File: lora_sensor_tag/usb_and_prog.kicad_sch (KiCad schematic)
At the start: 0 parts

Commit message: lora_sensor_tag: Update shematic
Update schematic with the following changes:
 - Add SX1276 LoRa modem schematic;
 - Add antenna matching network for SX1276 LoRa modem;
 - Add PE4259 RF switch for SX1276 LoRa modem;
 - Add USB-C connector;
 - Add CP2102 USB-to-UART bridge and programming interface;

Signed-off-by: Volodymyr <volodymyrnoha99@gmail.com>
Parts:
- added C39: C, symbol Device:C
- added D1, D2, D3: 1N630xCA, Diode_THT:D_DO-201AE_P15.24mm_Horizontal, symbol Diode:1N630xCA
- added J3: USB_C_Receptacle_USB2.0_14P, Package_DFN_QFN:Texas_RNQ0040A_WQFN-40-1EP_6x4mm_P0.4mm_EP4.7x2.7mm, symbol Connector:USB_C_Receptacle_USB2.0_14P
- added Q1: NPN, Package_DFN_QFN:Nordic_AQFN-94-1EP_7x7mm_P0.4mm, symbol Simulation_SPICE:NPN
- added Q2: NPN, symbol Simulation_SPICE:NPN
- added R18, R19, R20, R21, R22, R23: R, Package_DFN_QFN:QFN-24-1EP_4x4mm_P0.5mm_EP2.6x2.6mm, symbol Device:R
- added U10: CP2102N-Axx-xQFN28, Package_DFN_QFN:QFN-28-1EP_5x5mm_P0.5mm_EP3.35x3.35mm, symbol Interface_USB:CP2102N-Axx-xQFN28
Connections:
- new net: Q1.2 (B), R22.2
- new net: R20.1, R21.2, U10.8 (VBUS)
- new net: Q2.2 (B), R23.2
- new net: R18.2, U10.9 (~{RST})
- new net: R19.1, U10.11 (~{SUSPEND})
- new net 3V3: C39.1, R18.1, U10.6 (VDD), U10.7 (VREGIN)
- new net DTR: Q2.3 (E), R22.1, U10.28 (~{DTR})
- new net GND: C39.2, D1.1 (A1), D2.1 (A1), D3.1 (A1), J3.A1 (GND), J3.A12 (GND), J3.B1 (GND), J3.B12 (GND), J3.SH (SHIELD), R19.2, R21.1, U10.29 (GND), U10.3 (GND)
- new net MCU_EN: Q1.1 (C)
- new net MCU_IO0: Q2.1 (C)
- new net MCU_RX: U10.25 (RXD)
- new net MCU_TX: U10.26 (TXD)
- new net RTS: Q1.3 (E), R23.1, U10.24 (~{RTS})
- new net USB_D_M: D2.2 (A2), J3.A7 (D-), J3.B7 (D-), U10.5 (D-)
- new net USB_D_P: D1.2 (A2), J3.A6 (D+), J3.B6 (D+), U10.4 (D+)
- new net VUSB: D3.2 (A2), J3.A4 (VBUS), J3.A9 (VBUS), J3.B4 (VBUS), J3.B9 (VBUS), R20.2
- no-connect marks 0 -> 17
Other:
- note added: "Optional"
- note added: "UART-USB"
- note added: "USB-C"

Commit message: Update schematic notation and fix bugs
Global labels notation updated;
Swapped line order in schematic fixed;
Added pull-up resistor to PG-ALERT pin (fuel gauge)

Signed-off-by: Volodymyr <volodymyrnoha99@gmail.com>
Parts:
- renumbered R18 to R19, R19 to R22, R22 to R23, R23 to R24, U10 to U9
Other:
- title: (none) -> USB and programmer
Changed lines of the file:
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@@
 	(generator_version "10.0")
 	(paper "A4")
+	(title_block
+		(title "USB and programmer")
+		(rev "1.0")
+	)
 	(rectangle
 		(start 104.14 24.13)
@@
 	)
 	(hierarchical_label "MCU_EN"
-		(shape input)
+		(shape output)
 		(at 148.59 118.11 0)
 		(effects
@@
 	)
 	(hierarchical_label "MCU_TX"
-		(shape input)
+		(shape output)
 		(at 208.28 50.8 0)
 		(effects
@@
 	)
 	(hierarchical_label "MCU_IO0"
-		(shape input)
+		(shape output)
 		(at 147.32 148.59 0)
 		(effects
@@
 		(in_pos_files yes)
 		(dnp no)
-		(property "Reference" "R22"
+		(property "Reference" "R23"
 			(at 121.92 120.904 90)
 			(show_name no)
@@
 			(project "lora_sensor_tag"
 				(path "/c36711c6-27c1-4315-8bea-60438d6eedb7/cc2abe59-c980-47ad-a0cf-32ea17a25214"
-					(reference "R22")
+					(reference "R23")
 					(unit 1)
 				)
@@
 		(in_pos_files yes)
 		(dnp no)
-		(property "Reference" "#PWR076"
+		(property "Reference" "#PWR070"
 			(at 175.26 45.72 0)
 			(hide yes)
@@
 			(project "lora_sensor_tag"
 				(path "/c36711c6-27c1-4315-8bea-60438d6eedb7/cc2abe59-c980-47ad-a0cf-32ea17a25214"
-					(reference "#PWR076")
+					(reference "#PWR070")
 					(unit 1)
 				)
@@
 		(dnp no)
 		(fields_autoplaced yes)
-		(property "Reference" "#PWR037"
+		(property "Reference" "#PWR069"
 			(at 74.93 39.37 0)
 			(hide yes)
@@
 			(project "lora_sensor_tag"
 				(path "/c36711c6-27c1-4315-8bea-60438d6eedb7/cc2abe59-c980-47ad-a0cf-32ea17a25214"
-					(reference "#PWR037")
+					(reference "#PWR069")
 					(unit 1)
 				)
@@
 		(in_pos_files yes)
 		(dnp no)
-		(property "Reference" "#PWR070"
+		(property "Reference" "#PWR073"
 			(at 68.58 71.12 0)
 			(hide yes)
@@
 			(project "lora_sensor_tag"
 				(path "/c36711c6-27c1-4315-8bea-60438d6eedb7/cc2abe59-c980-47ad-a0cf-32ea17a25214"
-					(reference "#PWR070")
+					(reference "#PWR073")
 					(unit 1)
 				)
@@
 		(in_pos_files yes)
 		(dnp no)
-		(property "Reference" "R23"
+		(property "Reference" "R24"
 			(at 121.412 145.796 90)
 			(show_name no)
@@
 			(project "lora_sensor_tag"
 				(path "/c36711c6-27c1-4315-8bea-60438d6eedb7/cc2abe59-c980-47ad-a0cf-32ea17a25214"
-					(reference "R23")
+					(reference "R24")
 					(unit 1)
 				)
@@
 		(in_pos_files yes)
 		(dnp no)
-		(property "Reference" "#PWR073"
+		(property "Reference" "#PWR072"
 			(at 152.4 54.61 0)
 			(hide yes)
@@
 			(project "lora_sensor_tag"
 				(path "/c36711c6-27c1-4315-8bea-60438d6eedb7/cc2abe59-c980-47ad-a0cf-32ea17a25214"
-					(reference "#PWR073")
+					(reference "#PWR072")
 					(unit 1)
 				)
@@
 		(in_pos_files yes)
 		(dnp no)
-		(property "Reference" "R18"
+		(property "Reference" "R19"
 			(at 162.56 48.514 90)
 			(show_name no)
@@
 			(project "lora_sensor_tag"
 				(path "/c36711c6-27c1-4315-8bea-60438d6eedb7/cc2abe59-c980-47ad-a0cf-32ea17a25214"
-					(reference "R18")
+					(reference "R19")
 					(unit 1)
 				)
@@
 		(in_pos_files yes)
 		(dnp no)
-		(property "Reference" "#PWR075"
+		(property "Reference" "#PWR068"
 			(at 175.26 34.29 0)
 			(hide yes)
@@
 			(project "lora_sensor_tag"
 				(path "/c36711c6-27c1-4315-8bea-60438d6eedb7/cc2abe59-c980-47ad-a0cf-32ea17a25214"
-					(reference "#PWR075")
+					(reference "#PWR068")
 					(unit 1)
 				)
@@
 		(in_pos_files yes)
 		(dnp no)
-		(property "Reference" "#PWR074"
+		(property "Reference" "#PWR076"
 			(at 217.17 82.55 0)
 			(hide yes)
@@
 			(project "lora_sensor_tag"
 				(path "/c36711c6-27c1-4315-8bea-60438d6eedb7/cc2abe59-c980-47ad-a0cf-32ea17a25214"
-					(reference "#PWR074")
+					(reference "#PWR076")
 					(unit 1)
 				)
@@
 		(in_pos_files yes)
 		(dnp no)
-		(property "Reference" "#PWR071"
+		(property "Reference" "#PWR077"
 			(at 184.15 119.38 0)
 			(hide yes)
@@
 			(project "lora_sensor_tag"
 				(path "/c36711c6-27c1-4315-8bea-60438d6eedb7/cc2abe59-c980-47ad-a0cf-32ea17a25214"
-					(reference "#PWR071")
+					(reference "#PWR077")
 					(unit 1)
 				)
@@
 		(in_pos_files yes)
 		(dnp no)
-		(property "Reference" "#PWR068"
+		(property "Reference" "#PWR074"
 			(at 36.83 81.28 0)
 			(hide yes)
@@
 			(project "lora_sensor_tag"
 				(path "/c36711c6-27c1-4315-8bea-60438d6eedb7/cc2abe59-c980-47ad-a0cf-32ea17a25214"
-					(reference "#PWR068")
+					(reference "#PWR074")
 					(unit 1)
 				)
@@
 		(in_pos_files yes)
 		(dnp no)
-		(property "Reference" "#PWR077"
+		(property "Reference" "#PWR075"
 			(at 144.78 82.55 0)
 			(hide yes)
@@
 			(project "lora_sensor_tag"
 				(path "/c36711c6-27c1-4315-8bea-60438d6eedb7/cc2abe59-c980-47ad-a0cf-32ea17a25214"
-					(reference "#PWR077")
+					(reference "#PWR075")
 					(unit 1)
 				)
@@
 		(in_pos_files yes)
 		(dnp no)
-		(property "Reference" "R19"
+		(property "Reference" "R22"
 			(at 210.82 73.914 90)
 			(show_name no)
@@
 			(project "lora_sensor_tag"
 				(path "/c36711c6-27c1-4315-8bea-60438d6eedb7/cc2abe59-c980-47ad-a0cf-32ea17a25214"
-					(reference "R19")
+					(reference "R22")
 					(unit 1)
 				)
@@
 		(in_pos_files yes)
 		(dnp no)
-		(property "Reference" "#PWR078"
+		(property "Reference" "#PWR071"
 			(at 144.78 54.61 0)
 			(hide yes)
@@
 			(project "lora_sensor_tag"
 				(path "/c36711c6-27c1-4315-8bea-60438d6eedb7/cc2abe59-c980-47ad-a0cf-32ea17a25214"
-					(reference "#PWR078")
+					(reference "#PWR071")
 					(unit 1)
 				)
@@
 		(in_pos_files yes)
 		(dnp no)
-		(property "Reference" "U10"
+		(property "Reference" "U9"
 			(at 188.214 110.744 0)
 			(show_name no)
@@
 			(project "lora_sensor_tag"
 				(path "/c36711c6-27c1-4315-8bea-60438d6eedb7/cc2abe59-c980-47ad-a0cf-32ea17a25214"
-					(reference "U10")
+					(reference "U9")
 					(unit 1)
 				)

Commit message: Bug fixing
The following bugs and issues have been fixed:
- Fixed LoRa Rx\Tx line polarity;
- Removed unnneccessary pull-up\pull-down resistors;
- Added pull-up resistor to IO0;
- Added resistive divider for MCP7387 VPCC pin;
- GPIO_SEL moved from IO4 to IO26 (IO4 used for flash init and can cause unexpected behavior);
- CC1 and CC2 of USB-C port connected to GND via pull-down resistors;

Signed-off-by: Volodymyr <volodymyrnoha99@gmail.com>
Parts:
- added R25, R26: 5K1, Package_DFN_QFN:QFN-24-1EP_4x4mm_P0.5mm_EP2.6x2.6mm, symbol Device:R
- added R27: 10K, Package_DFN_QFN:QFN-24-1EP_4x4mm_P0.5mm_EP2.6x2.6mm, symbol Device:R
- R22: value R -> NC
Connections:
- net 3V3: now also R27.2
- net GND: now also R25.1, R26.1
- net MCU_IO0: now also R27.1
- net MCU_RX: now also U9.26 (TXD); no longer U9.25 (RXD)
- net MCU_TX: now also U9.25 (RXD); no longer U9.26 (TXD)
- net at J3.A5 (CC1): now also R25.2
- net at J3.B5 (CC2): now also R26.2
- no-connect marks 17 -> 15
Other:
- note added: "CC1 and CC2 are the Configuration Channel pins on a USB Type-C connector used to detect plug orientation, establish host-to-device roles, and negotiate power"

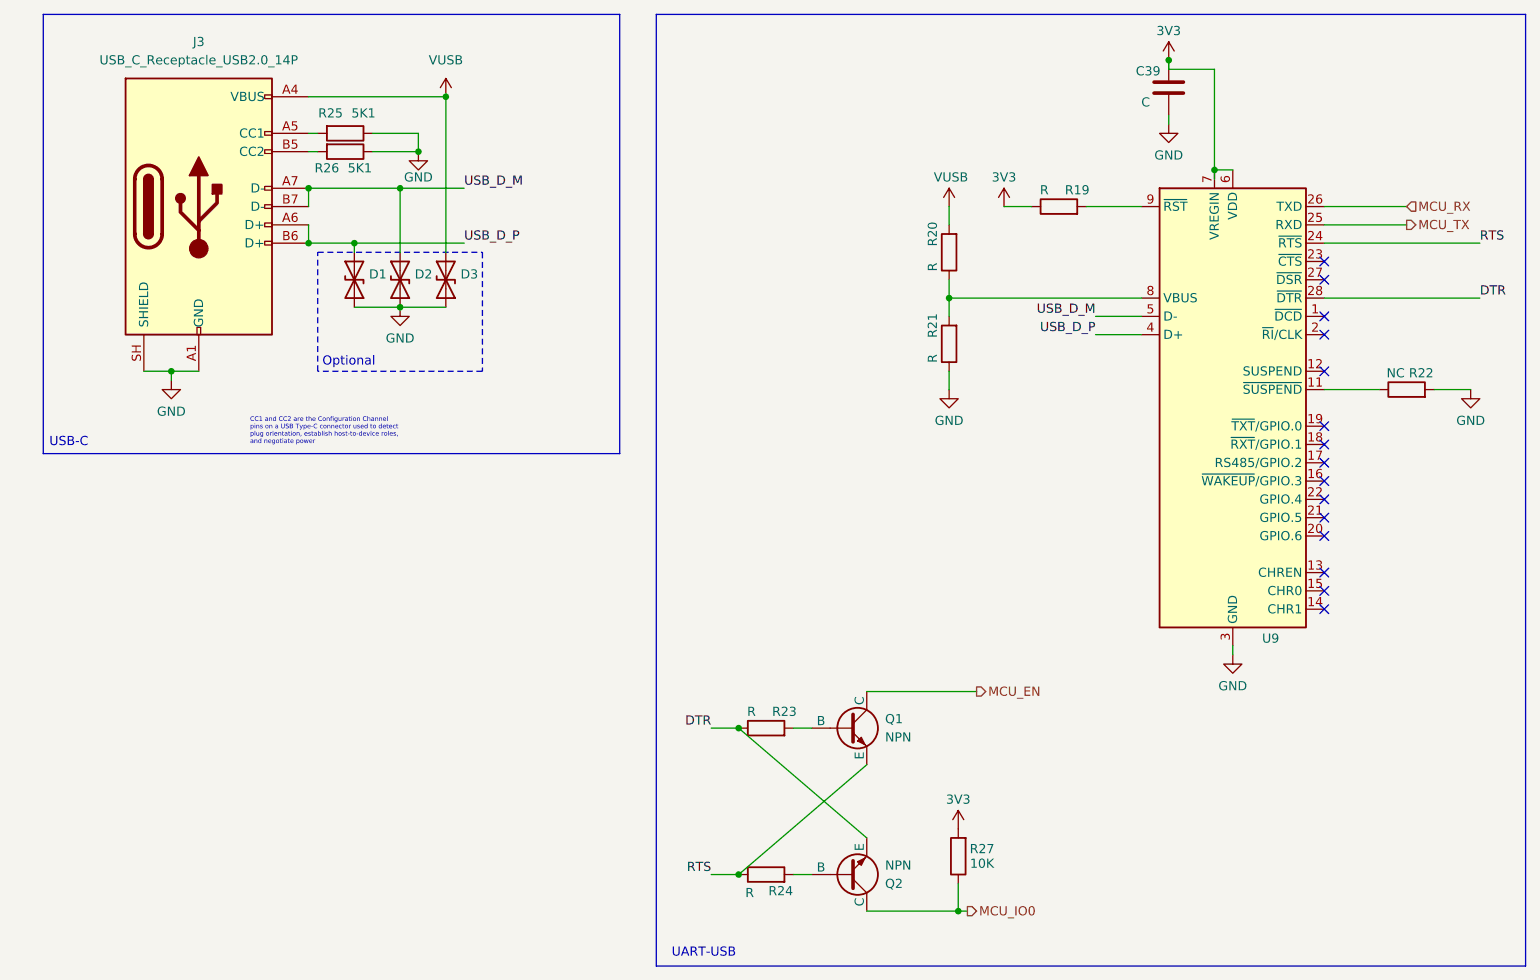
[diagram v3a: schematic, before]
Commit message: Large schematic update
This commit update the following:

 - Update MCP73871 CE control schematic
 - Finished schematic development and footprint
   assignment

Signed-off-by: Volodymyr <volodymyrnoha99@gmail.com>
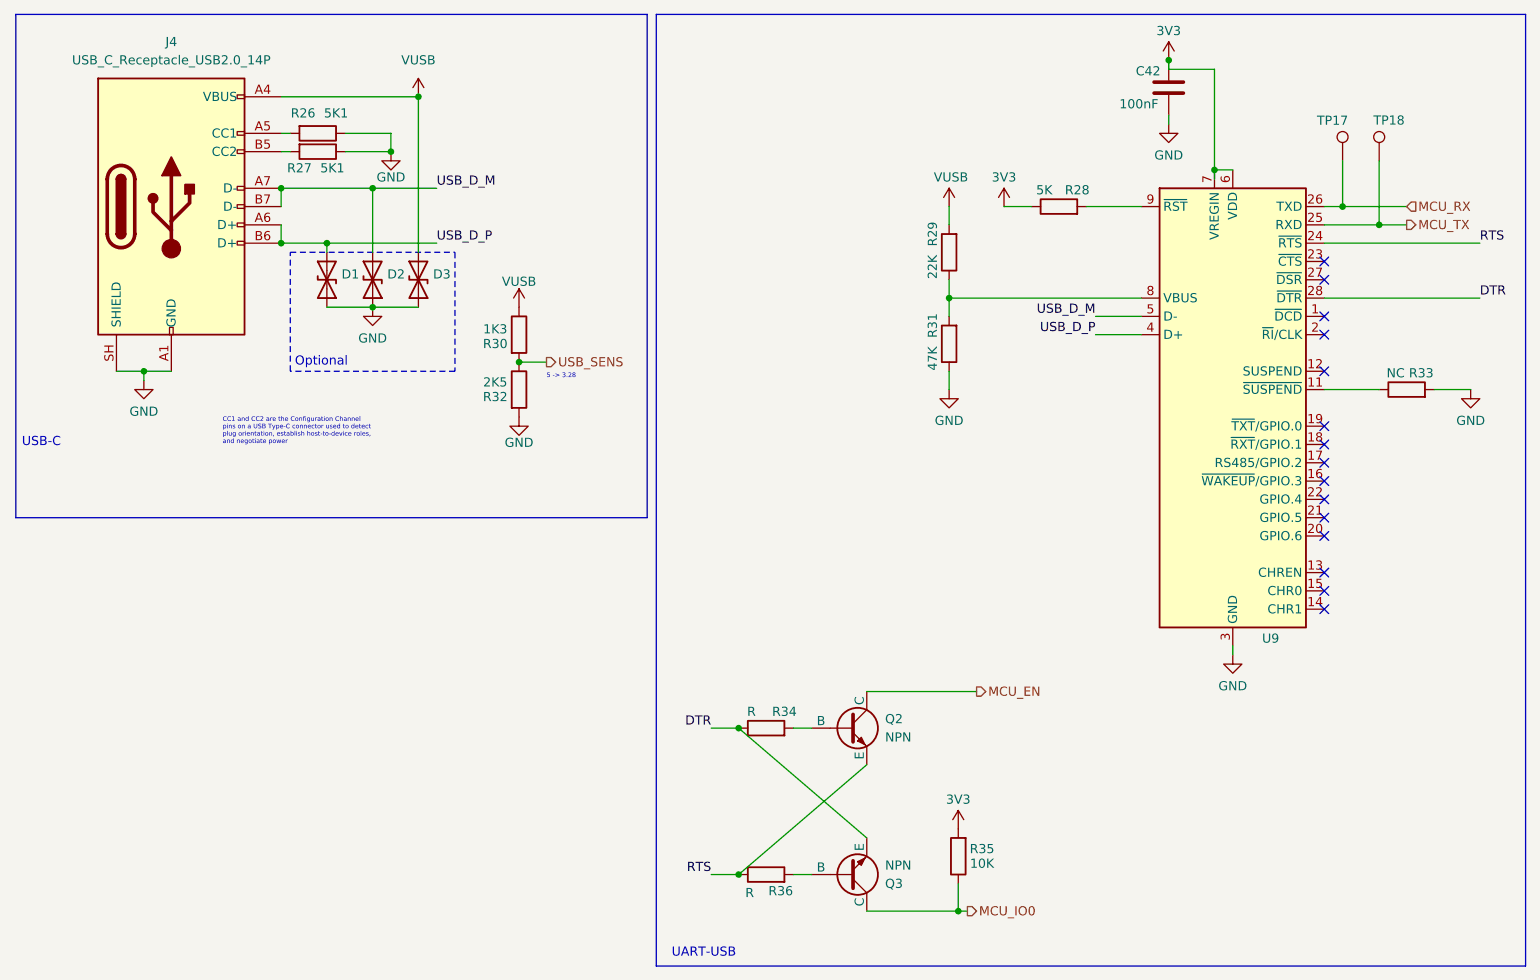
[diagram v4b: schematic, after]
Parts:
- added R30: 1K3, Resistor_SMD:R_0603_1608Metric, symbol Device:R
- added R32: 2K5, Resistor_SMD:R_0603_1608Metric, symbol Device:R
- added TP17, TP18: TestPoint, TestPoint:TestPoint_Pad_D1.0mm, symbol Connector:TestPoint
- C42: renamed from C39; value C -> 100nF; footprint (none) -> Capacitor_SMD:C_0603_1608Metric
- D1, D2, D3: footprint Diode_THT:D_DO-201AE_P15.24mm_Horizontal -> Diode_SMD:D_0603_1608Metric
- J4: renamed from J3; footprint Package_DFN_QFN:Texas_RNQ0040A_WQFN-40-1EP_6x4mm_P0.4mm_EP4.7x2.7mm -> Connector_USB:USB_C_Receptacle_XKB_U262-16XN-4BVC11
- Q2: renamed from Q1; footprint Package_DFN_QFN:Nordic_AQFN-94-1EP_7x7mm_P0.4mm -> Package_TO_SOT_SMD:SOT-23
- Q3: renamed from Q2; footprint (none) -> Package_TO_SOT_SMD:SOT-23
- R26: renamed from R25; footprint Package_DFN_QFN:QFN-24-1EP_4x4mm_P0.5mm_EP2.6x2.6mm -> Resistor_SMD:R_0603_1608Metric
- R27: renamed from R26; footprint Package_DFN_QFN:QFN-24-1EP_4x4mm_P0.5mm_EP2.6x2.6mm -> Resistor_SMD:R_0603_1608Metric
- R28: renamed from R19; value R -> 5K; footprint Package_DFN_QFN:QFN-24-1EP_4x4mm_P0.5mm_EP2.6x2.6mm -> Resistor_SMD:R_0603_1608Metric
- R29: renamed from R20; value R -> 22K; footprint Package_DFN_QFN:QFN-24-1EP_4x4mm_P0.5mm_EP2.6x2.6mm -> Resistor_SMD:R_0603_1608Metric
- R31: renamed from R21; value R -> 47K; footprint Package_DFN_QFN:QFN-24-1EP_4x4mm_P0.5mm_EP2.6x2.6mm -> Resistor_SMD:R_0603_1608Metric
- R33: renamed from R22; footprint Package_DFN_QFN:QFN-24-1EP_4x4mm_P0.5mm_EP2.6x2.6mm -> Resistor_SMD:R_0603_1608Metric
- R34: renamed from R23; footprint Package_DFN_QFN:QFN-24-1EP_4x4mm_P0.5mm_EP2.6x2.6mm -> Resistor_SMD:R_0603_1608Metric
- R35: renamed from R27; footprint Package_DFN_QFN:QFN-24-1EP_4x4mm_P0.5mm_EP2.6x2.6mm -> Resistor_SMD:R_0603_1608Metric
- R36: renamed from R24; footprint Package_DFN_QFN:QFN-24-1EP_4x4mm_P0.5mm_EP2.6x2.6mm -> Resistor_SMD:R_0603_1608Metric
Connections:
- net GND: now also R32.2
- net MCU_RX: now also TP17.1
- net MCU_TX: now also TP18.1
- net VUSB: now also R30.1
- new net USB_SENS: R30.2, R32.1
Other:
- note added: "5 -> 3.28"
- moved on the sheet: D1, D2, D3, J4, R26, R27

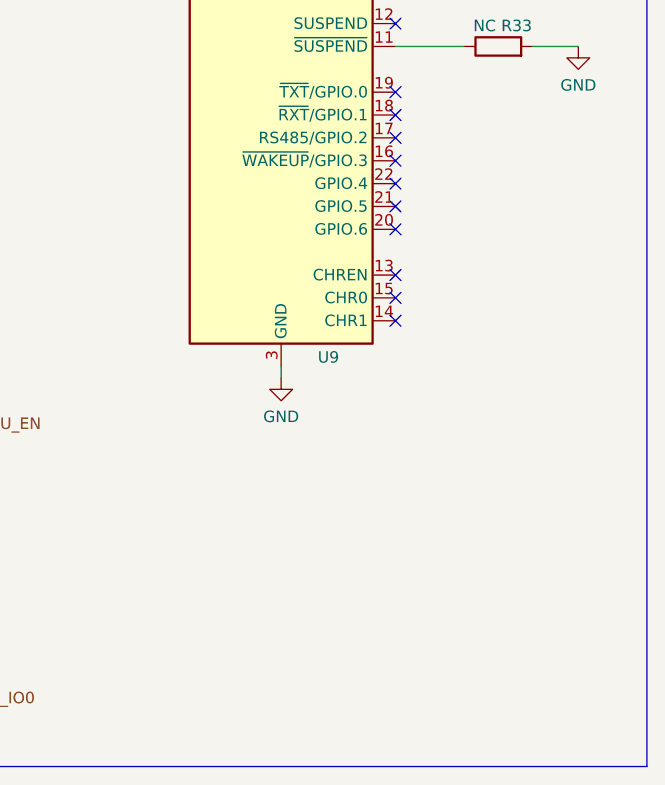
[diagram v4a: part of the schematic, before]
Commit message: Update schematics
Adds the following updates to the schematics:
- Add power switch to the device;
- Add various LED indicators for device status monitoring;
- Add Reset and Prog buttons for device control;

Signed-off-by: Volodymyr <volodymyrnoha99@gmail.com>
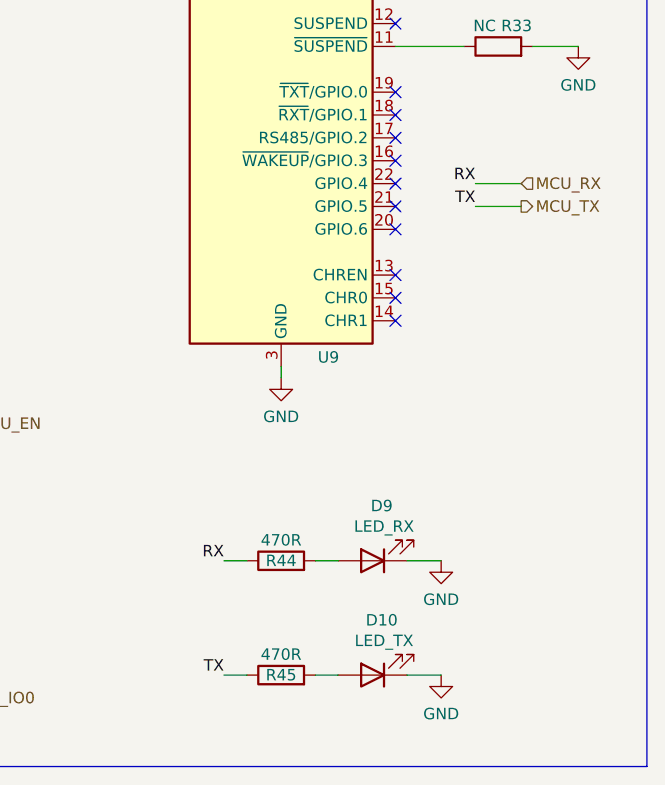
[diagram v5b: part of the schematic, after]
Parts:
- added D10: LED_TX, LED_SMD:LED_0603_1608Metrica, symbol Device:LED
- added D9: LED_RX, LED_SMD:LED_0603_1608Metrica, symbol Device:LED
- added R44, R45: 470R, Resistor_SMD:R_0603_1608Metric, symbol Device:R
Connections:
- net GND: now also D10.1 (K), D9.1 (K)
- net MCU_RX: now also R44.1
- net MCU_TX: now also R45.1
- new net: D10.2 (A), R45.2
- new net: D9.2 (A), R44.2

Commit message: pcb_layout: Add initial board layout
Adds:
 - Initial board dimensions;
 - Initial MCU component placement and routing

Signed-off-by: Volodymyr <volodymyrnoha99@gmail.com>
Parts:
- renumbered C42 to C44, D1 to D6, D2 to D7, D3 to D8, R26 to R33, R27 to R34, R28 to R35, R29 to R36, R30 to R37, R31 to R38, R32 to R39, R33 to R40, R34 to R41, R44 to R42, R35 to R43, R36 to R44

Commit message: Add USB and CP2102 initial layout
Signed-off-by: Volodymyr <volodymyrnoha99@gmail.com>
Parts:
- D10, D9: footprint LED_SMD:LED_0603_1608Metrica -> LED_SMD:LED_0603_1608Metric
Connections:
- net USB_D_M renamed USB_D_N
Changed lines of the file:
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@@
 		)
 	)
-	(label "USB_D_M"
+	(label "USB_D_N"
 		(at 73.66 48.26 0)
 		(effects
@@
 		)
 	)
-	(label "USB_D_M"
+	(label "USB_D_N"
 		(at 165.1 66.04 180)
 		(effects
@@
 			)
 		)
-		(property "Footprint" "LED_SMD:LED_0603_1608Metrica"
+		(property "Footprint" "LED_SMD:LED_0603_1608Metric"
 			(at 194.31 146.05 0)
 			(hide yes)
@@
 			)
 		)
-		(property "Footprint" "LED_SMD:LED_0603_1608Metrica"
+		(property "Footprint" "LED_SMD:LED_0603_1608Metric"
 			(at 194.31 133.35 0)
 			(hide yes)

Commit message: Update PCB layout routing
Updates and adds the following changes to the PCB
layout routing:
- Changed board dimensions and topology;
- Add layout for MCP73871 Li-ion battery charger;
- Add layout for MAX17048 Fuel Gauge;

Signed-off-by: Volodymyr <volodymyrnoha99@gmail.com>
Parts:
- added H1, H2, H3, H4: MountingHole, MountingHole:MountingHole_2.1mm, symbol Mechanical:MountingHole
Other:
- note added: "Mounting points"
